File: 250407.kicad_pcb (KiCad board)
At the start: 2 copper layers, 390 x 179.8 mm, 227 parts, among them CN1 KEYBOARD_20PIN_MALE, CN10 LED_CONNECTOR, CN2 USER_PORT_CON, CN3 CASSETTE_PORT_CON, CN4 SERIAL_BUS_CON, CN5 AV_CONN, CN6 EXPANSION_PORT, CN7 POWER_CON, CN8 CONTROL_PORT, CN9 CONTROL_PORT, M1 MODULATOR_LONGBOARD, Q1 2SC1815, Q2 2SC1815, Q3 TP29B/2SD880, Q7 2SC1815, Q8 2SC1815, SW1 POWER_SWITCH, U1 CIA_U1, U10 4164-2, U11 4164-2, U12 4164-2, U13 74LS257, U14 74LS258, U15 74LS139, U16 4066_U28, U17 PLA_U17, U18 6581, U19 VIC, U2 CIA_U2, U20 556, U21 4164-2, U22 4164-2, U23 4164-2, U24 4164-2, U25 74LS257, U26 74LS373, U27 7408_U27, U28 4066_U28, U29 74LS74, U3 2364A, U30 74LS193, U31 74LS629N, U32 MC4044, U4 2364A, U5 2332A, U6 2114, U7 6510_MPU, U8 7406N, U9 4164-2, Y1 Crystal

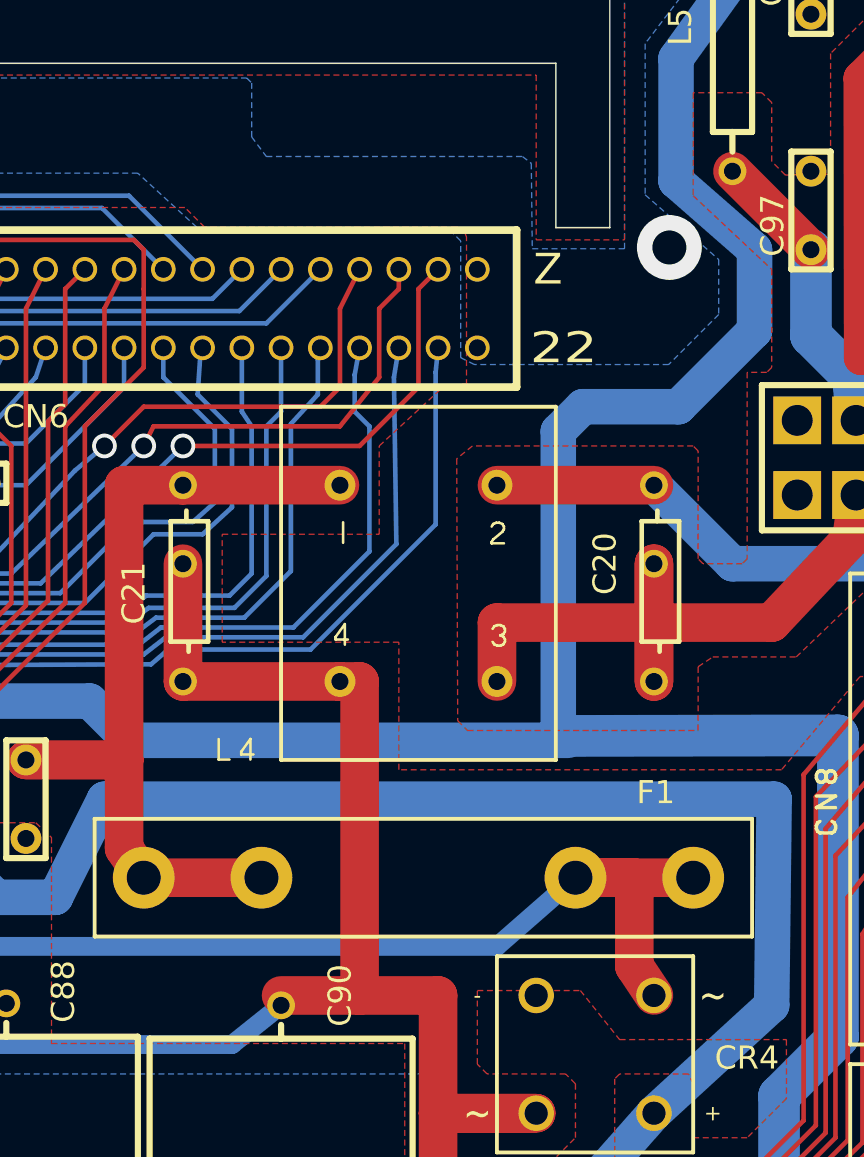
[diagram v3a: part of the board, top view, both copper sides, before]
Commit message: add several 3D models update footprints and PCB
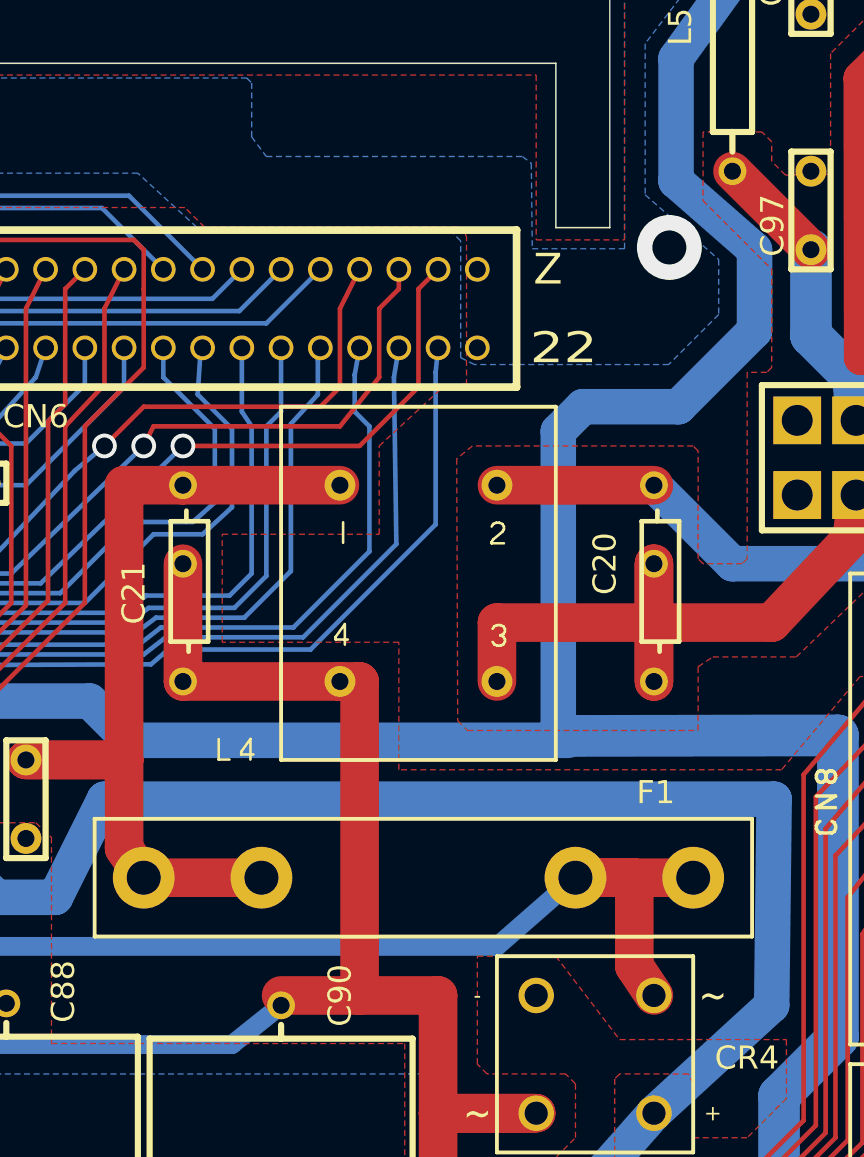
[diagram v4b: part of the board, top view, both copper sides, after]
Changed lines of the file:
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@@
   (general
     (thickness 1.6)
-    (drawings 3326)
+    (drawings 3322)
     (tracks 7093)
     (zones 0)
@@
   )
   (layers
-    (0 F.Cu signal)
-    (31 B.Cu signal hide)
+    (0 F.Cu signal hide)
+    (31 B.Cu signal)
     (32 B.Adhes user)
     (33 F.Adhes user)
@@
     (add_net ~VA15~)
   )
+  (module C64-pcb-library:FUSE (layer F.Cu)
+    (at 374.65 122.555 270)
+    (fp_text reference F1 (at -5.5115 2.423 180) (layer F.SilkS)
+      (effects (font (size 1.5 1.5) (thickness 0.25)))
+    )
+    (fp_text value 1A (at 0 -0.5 90) (layer F.Fab)
+      (effects (font (size 1 1) (thickness 0.15)))
+    )
+    (fp_line (start 3.81 38.735) (end 3.81 -3.81) (layer F.SilkS) (width 0.25))
+    (fp_line (start -3.81 38.735) (end 3.81 38.735) (layer F.SilkS) (width 0.25))
+    (fp_line (start -3.81 -3.81) (end -3.81 38.735) (layer F.SilkS) (width 0.25))
+    (fp_line (start 3.81 -3.81) (end -3.81 -3.81) (layer F.SilkS) (width 0.25))
+    (pad 2 thru_hole circle (at 0 35.56 270) (size 4 4) (drill 2.2) (layers *.Cu *.Mask)
+      (net 227 "Net-(C21-Pad1)"))
+    (pad 2 thru_hole circle (at 0 27.94 270) (size 4 4) (drill 2.2) (layers *.Cu *.Mask)
+      (net 227 "Net-(C21-Pad1)"))
+    (pad 1 thru_hole circle (at 0 7.62 270) (size 4 4) (drill 2.2) (layers *.Cu *.Mask)
+      (net 23 /'9VAC~~))
+    (pad 1 thru_hole circle (at 0 0 270) (size 4 4) (drill 2.2) (layers *.Cu *.Mask)
+      (net 23 /'9VAC~~))
+  )
   (module C64-pcb-library:BRIDGE_RECTIFIER (layer F.Cu)
     (at 372.11 137.795 270)
@@
     )
   )
-  (module C64-pcb-library:FUSE (layer F.Cu)
-    (at 374.65 122.555 270)
-    (fp_text reference F1 (at -5.5115 2.423 180) (layer F.SilkS)
-      (effects (font (size 1.5 1.5) (thickness 0.25)))
-    )
-    (fp_text value 1A (at 0 -0.5 90) (layer F.Fab)
-      (effects (font (size 1 1) (thickness 0.15)))
-    )
-    (pad 2 thru_hole circle (at 0 35.56 270) (size 4 4) (drill 2.2) (layers *.Cu *.Mask)
-      (net 227 "Net-(C21-Pad1)"))
-    (pad 2 thru_hole circle (at 0 27.94 270) (size 4 4) (drill 2.2) (layers *.Cu *.Mask)
-      (net 227 "Net-(C21-Pad1)"))
-    (pad 1 thru_hole circle (at 0 7.62 270) (size 4 4) (drill 2.2) (layers *.Cu *.Mask)
-      (net 23 /'9VAC~~))
-    (pad 1 thru_hole circle (at 0 0 270) (size 4 4) (drill 2.2) (layers *.Cu *.Mask)
-      (net 23 /'9VAC~~))
-  )
   (module C64-pcb-library:ZENER_12.7mm (layer F.Cu)
     (at 102.87 94.615 180)
@@
   (gr_line (start 140.5332 102.8327) (end 140.3466 102.7549) (layer F.SilkS) (width 0.222))
   (gr_line (start 140.3466 102.7549) (end 140.2532 102.5994) (layer F.SilkS) (width 0.222))
-  (gr_line (start 335.915 118.745) (end 378.46 118.745) (layer F.SilkS) (width 0.25))
-  (gr_line (start 378.46 118.745) (end 378.46 126.365) (layer F.SilkS) (width 0.25))
-  (gr_line (start 378.46 126.365) (end 335.915 126.365) (layer F.SilkS) (width 0.25))
-  (gr_line (start 335.915 126.365) (end 335.915 118.745) (layer F.SilkS) (width 0.25))
   (gr_line (start 365.76 92.075) (end 347.98 92.075) (layer F.SilkS) (width 0.25))
   (gr_line (start 347.98 92.075) (end 347.98 114.935) (layer F.SilkS) (width 0.25))
@@
         (xy 359.156 148.336) (xy 362.0135 148.336) (xy 361.95 150.495) (xy 364.49 150.495) (xy 364.49 141.9225)
         (xy 367.03 139.3825) (xy 367.03 135.89) (xy 366.395 135.255) (xy 361.315 135.255) (xy 360.68 134.62)
-        (xy 360.68 129.8575) (xy 367.3475 129.8575) (xy 369.8875 133.0325) (xy 380.6825 133.0325) (xy 380.6825 136.8425)
+        (xy 360.68 127.635) (xy 365.76 127.635) (xy 369.8875 133.0325) (xy 380.6825 133.0325) (xy 380.6825 136.8425)
         (xy 378.1425 139.3825) (xy 374.65 139.3825) (xy 374.65 135.89) (xy 374.3325 135.255) (xy 369.8875 135.255)
         (xy 369.57 135.5725) (xy 369.57 142.24) (xy 369.8875 143.1925) (xy 374.65 143.1925) (xy 374.65 188.2775)
@@
       (pts
         (xy 386.08 66.675) (xy 383.54 69.215) (xy 383.54 77.0255) (xy 382.0795 77.0255) (xy 380.619 77.089)
-        (xy 379.73 76.2) (xy 379.73 72.39) (xy 379.095 71.755) (xy 374.65 71.755) (xy 374.65 78.4225)
+        (xy 379.73 76.2) (xy 379.73 74.93) (xy 379.095 74.295) (xy 375.285 74.295) (xy 375.285 78.74)
         (xy 379.73 83.185) (xy 379.73 89.535) (xy 379.4125 89.8525) (xy 378.1425 89.8525) (xy 378.1425 101.9175)
         (xy 377.825 102.235) (xy 375.285 102.235) (xy 374.9675 101.9175) (xy 374.9675 94.9325) (xy 374.65 94.615)
